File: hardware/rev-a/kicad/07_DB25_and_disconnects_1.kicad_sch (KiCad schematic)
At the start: 16 parts

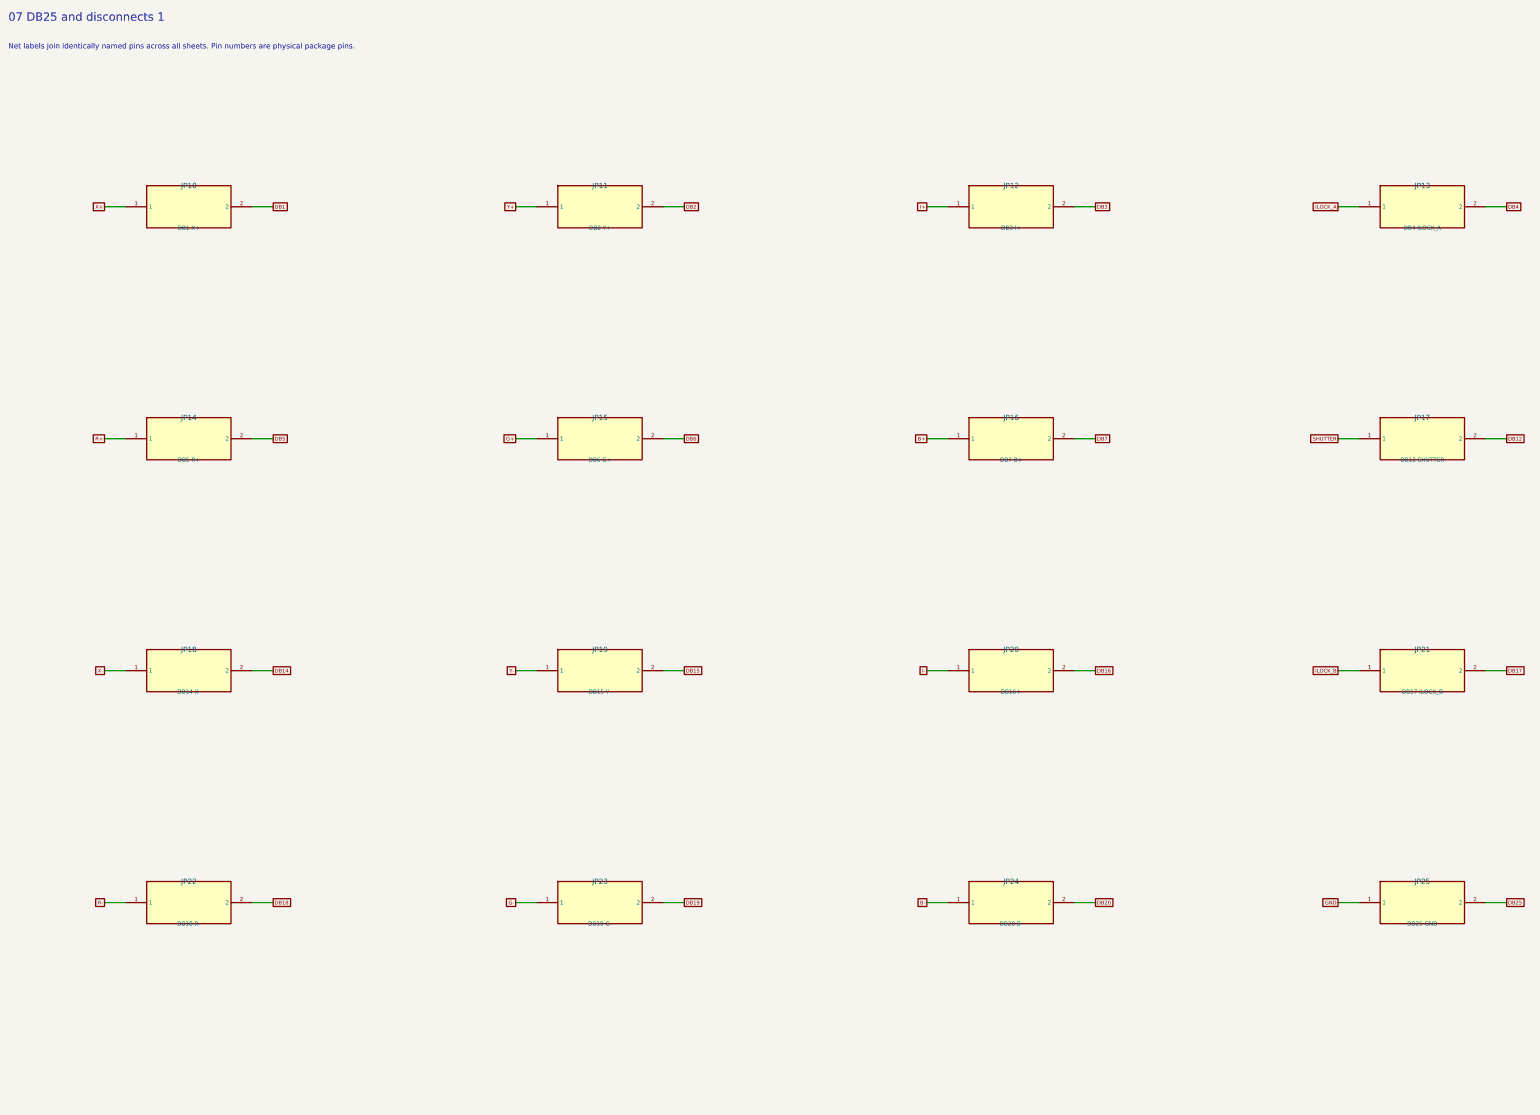
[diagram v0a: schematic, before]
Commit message: Redraw Rev.A schematics with functional blocks and explicit wiring
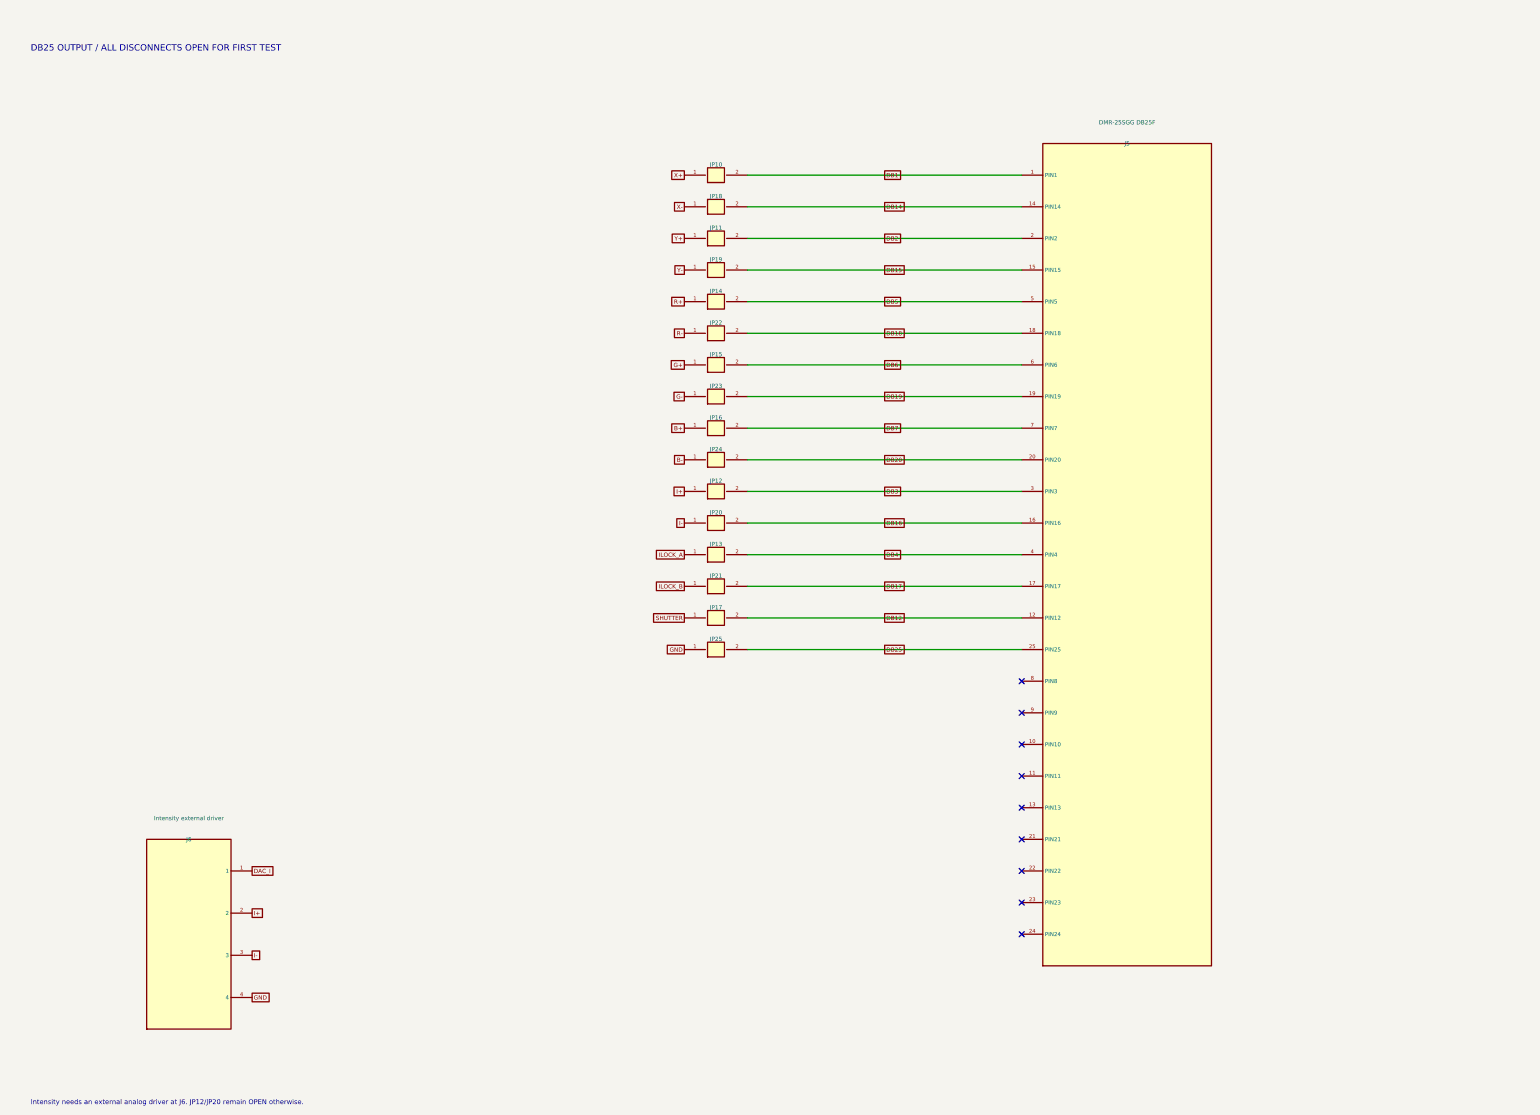
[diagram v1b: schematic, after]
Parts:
- added J5: DMR-25SGG DB25F, RevA:DMR25SGG, symbol RevA:Part_J5
- added J6: Intensity external driver, RevA:PinHeader_1x04_P2.54mm_Vertical, symbol RevA:Part_J6
- JP10: symbol RevA:Conn_JP10 -> RevA:Link
- JP11: symbol RevA:Conn_JP11 -> RevA:Link
- JP12: symbol RevA:Conn_JP12 -> RevA:Link
- JP13: symbol RevA:Conn_JP13 -> RevA:Link
- JP14: symbol RevA:Conn_JP14 -> RevA:Link
- JP15: symbol RevA:Conn_JP15 -> RevA:Link
- JP16: symbol RevA:Conn_JP16 -> RevA:Link
- JP17: symbol RevA:Conn_JP17 -> RevA:Link
- JP18: symbol RevA:Conn_JP18 -> RevA:Link
- JP19: symbol RevA:Conn_JP19 -> RevA:Link
- JP20: symbol RevA:Conn_JP20 -> RevA:Link
- JP21: symbol RevA:Conn_JP21 -> RevA:Link
- JP22: symbol RevA:Conn_JP22 -> RevA:Link
- JP23: symbol RevA:Conn_JP23 -> RevA:Link
- JP24: symbol RevA:Conn_JP24 -> RevA:Link
- JP25: symbol RevA:Conn_JP25 -> RevA:Link
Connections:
- net DB1: now also J5.1 (PIN1)
- net DB12: now also J5.12 (PIN12)
- net DB14: now also J5.14 (PIN14)
- net DB15: now also J5.15 (PIN15)
- net DB16: now also J5.16 (PIN16)
- net DB17: now also J5.17 (PIN17)
- net DB18: now also J5.18 (PIN18)
- net DB19: now also J5.19 (PIN19)
- net DB2: now also J5.2 (PIN2)
- net DB20: now also J5.20 (PIN20)
- net DB25: now also J5.25 (PIN25)
- net DB3: now also J5.3 (PIN3)
- net DB4: now also J5.4 (PIN4)
- net DB5: now also J5.5 (PIN5)
- net DB6: now also J5.6 (PIN6)
- net DB7: now also J5.7 (PIN7)
- net GND: now also J6.4
- net I+: now also J6.2
- net I-: now also J6.3
- new net DAC_I: J6.1
- no-connect marks 0 -> 9
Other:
- note added: "DB25 OUTPUT / ALL DISCONNECTS OPEN FOR FIRST TEST"
- note added: "Intensity needs an external analog driver at J6. JP12/JP20 remain OPEN otherwise."
- note removed: "07 DB25 and disconnects 1"
- note removed: "Net labels join identically named pins across all sheets. Pin numbers are physical package pins."
- company: CoreS3 ILDA evaluation -> (none)
- title: 07_DB25_and_disconnects_1 -> 12 / DB25 output and disconnect jumpers
